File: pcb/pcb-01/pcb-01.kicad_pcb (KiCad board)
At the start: 4 copper layers, 78 x 58 mm, 167 parts, among them J1 POWER, J2 MOTOR, J3 HALL, J4 TEMP, J5 I2C, J6 USB-C, J7 PROGRAM, J8 DNP 2x5 1.27mm, Q1 DMP6023LE-13, Q2 2N7002K, Q3 2N7002, SW1 SW_Push, SW2 SW_Push, SW3 SW_Push, U1 MCF8316DVRGFR, U10 SN74LVC1G17DCKR, U11 SN74LVC1G17DCKR, U12 TPD2EUSB30, U2 ESP32-C6-MINI-1, U3 TPSM365R6V3RDNR, U4 TPS7A1601DGN, U5 SN74LVC1G74DCTR, U6 SN74LVC1G74DCTR, U7 TPS3435CAKAGDD, U8 LM2907M-14, U9 TLV1701DBV

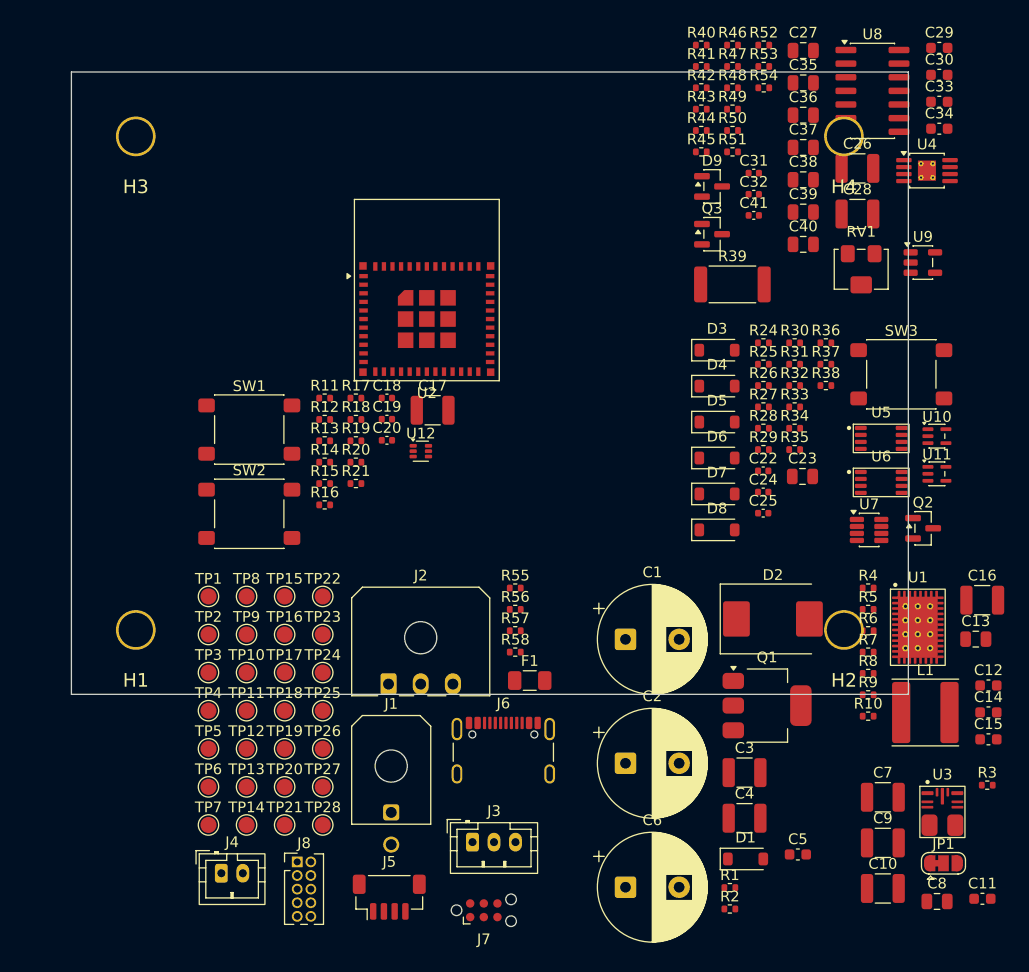
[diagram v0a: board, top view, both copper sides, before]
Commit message: pcb: placement checkpoint - zones seeded, mid-migration to packed layout
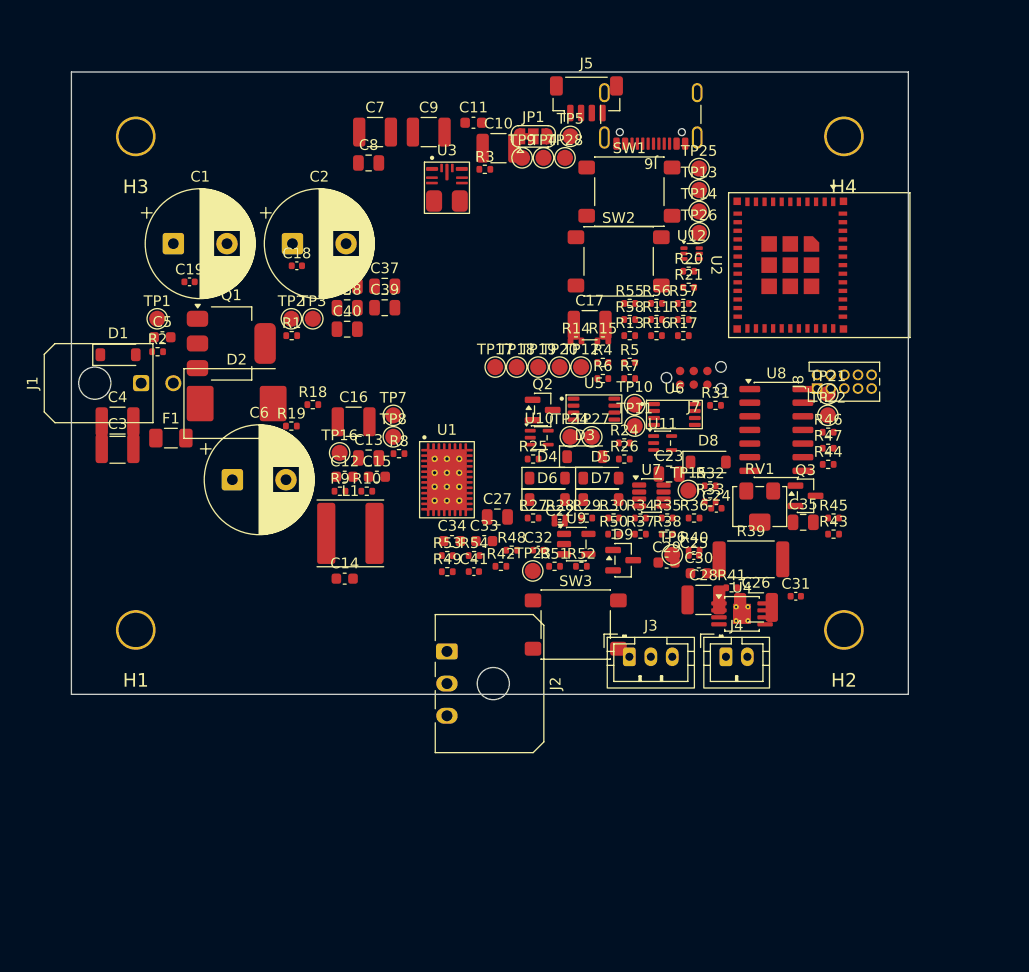
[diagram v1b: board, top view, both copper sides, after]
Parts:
- moved C8 86.9 mm to (77.7, 58.5)
- moved C11 86.5 mm to (87.5, 54.7)
- moved C9 78.6 mm to (83.3, 55.6)
- moved C7 78.0 mm to (78.3, 55.6)
- moved JP1 77.8 mm to (93.0, 56.0)
- moved C10 77.7 mm to (89.8, 57.1)
- moved J5 76.6 mm to (98.0, 52.5)
- moved C5 76.4 mm to (58.5, 74.7)
- moved D1 75.0 mm to (54.4, 76.3)
- moved R2 74.4 mm to (58.0, 76.1)
- moved U3 74.3 mm to (85.0, 61.0)
- moved R3 74.1 mm to (88.5, 59.1)
- moved TP14 71.0 mm to (108.5, 63.0)
- moved TP13 69.8 mm to (108.5, 61.0)
- moved C4 69.1 mm to (54.3, 82.6)
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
